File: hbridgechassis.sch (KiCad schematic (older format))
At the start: 8 parts, among them J1 Conn_01x02_Female, J2 Conn_01x02_Female, J3 Conn_01x02_Female, J4 Conn_01x07_Female, J5 Conn_01x02_Female, J6 Conn_01x02_Female, U1 L293DD

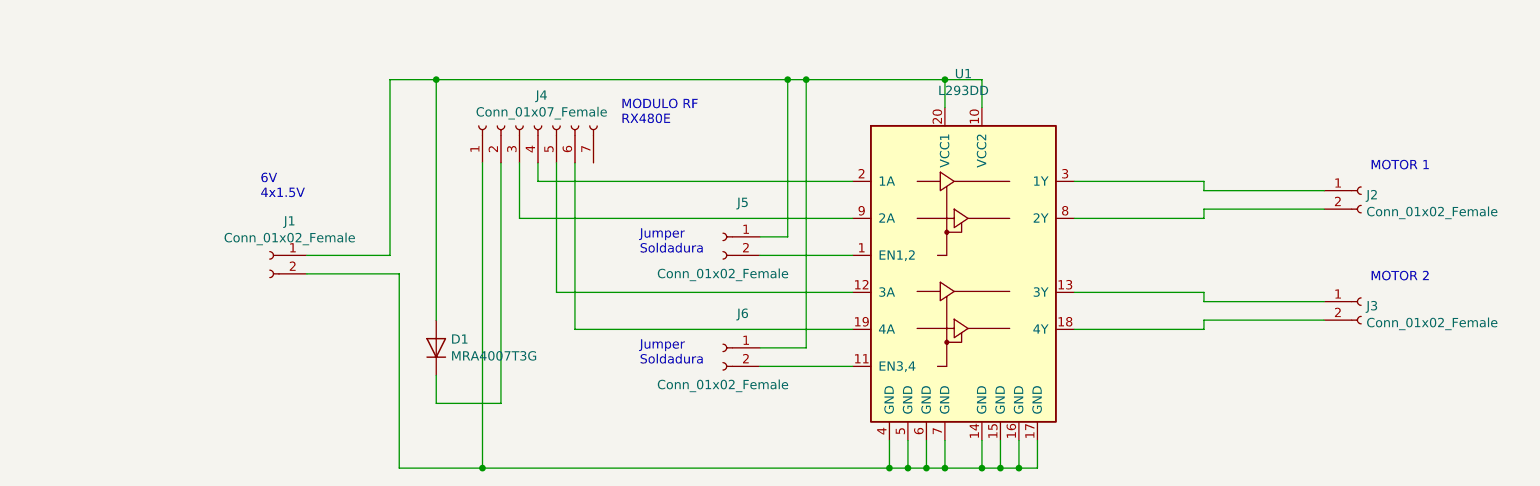
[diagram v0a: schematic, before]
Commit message: agregado regulador 78l05 y condensadores
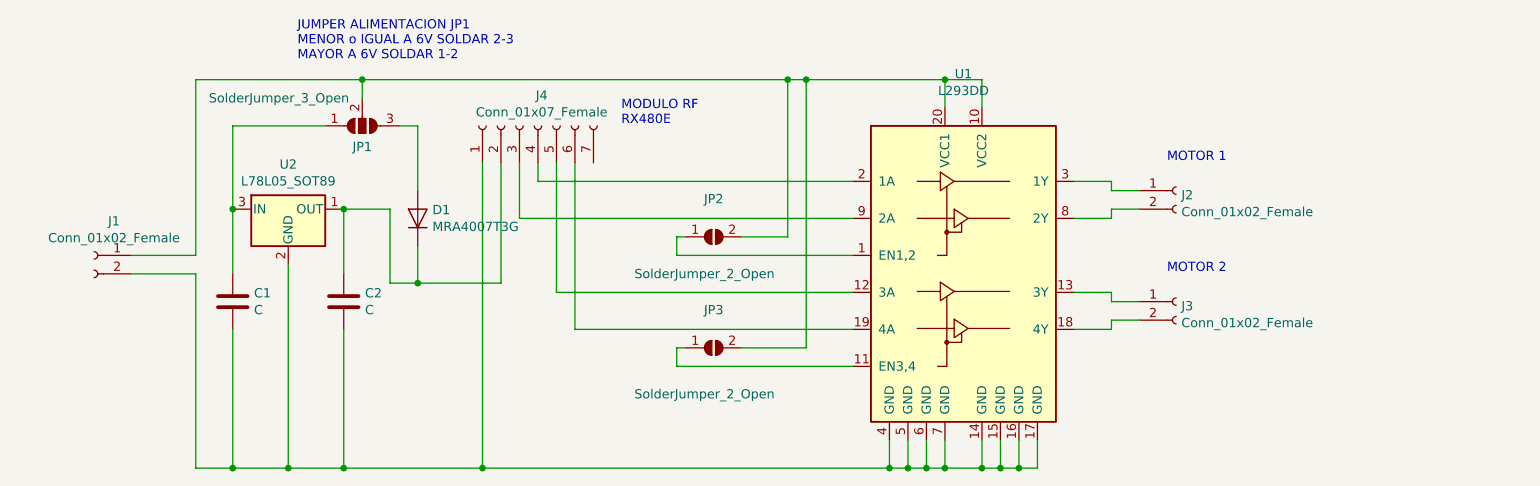
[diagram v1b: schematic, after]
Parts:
- removed J5, J6: Conn_01x02_Female, Jumper:SolderJumper-2_P1.3mm_Open_RoundedPad1.0x1.5mm, symbol Connector:Conn_01x02_Female
- added C1, C2: C, Capacitor_SMD:C_0805_2012Metric, symbol Device:C
- added JP1: SolderJumper_3_Open, Jumper:SolderJumper-3_P1.3mm_Open_RoundedPad1.0x1.5mm_NumberLabels, symbol Jumper:SolderJumper_3_Open
- added JP2, JP3: SolderJumper_2_Open, Jumper:SolderJumper-2_P1.3mm_Open_RoundedPad1.0x1.5mm, symbol Jumper:SolderJumper_2_Open
- added U2: L78L05_SOT89, Package_TO_SOT_SMD:SOT-89-3, symbol Regulator_Linear:L78L05_SOT89
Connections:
- net at U1.1 (EN1,2): now also JP2.1 (A)
- net at J1.1 (Pin_1), U1.10 (VCC2), U1.20 (VCC1): now also JP1.2 (C), JP2.2 (B), JP3.2 (B); no longer D1.2 (A)
- net at U1.11 (EN3,4): now also JP3.1 (A)
- net at J1.2 (Pin_2), J4.1 (Pin_1), U1.14 (GND)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: now also C1.2, C2.2, U2.2 (GND)
- net at D1.1 (K), J4.2 (Pin_2): now also C2.1, U2.1 (OUT)
- new net: C1.1, JP1.1 (A), U2.3 (IN)
- new net: D1.2 (A), JP1.3 (B)
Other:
- note added: "JUMPER ALIMENTACION JP1\nMENOR o IGUAL A 6V SOLDAR 2-3\nMAYOR A 6V SOLDAR 1-2"
- note removed: "6V \n4x1.5V"
- note removed: "Jumper\nSoldadura"
- moved on the sheet: D1, J1, J2, J3
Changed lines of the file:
@@
 L Connector:Conn_01x02_Female J1
 U 1 1 6009FC05
-P 1700 3500
-F 0 "J1" H 1592 3685 50  0000 C CNN
-F 1 "Conn_01x02_Female" H 1592 3594 50  0000 C CNN
-F 2 "TerminalBlock_4Ucon:TerminalBlock_4Ucon_1x02_P3.50mm_Horizontal" H 1700 3500 50  0001 C CNN
-F 3 "~" H 1700 3500 50  0001 C CNN
-	1    1700 3500
+P 750 3500
+F 0 "J1" H 642 3685 50  0000 C CNN
+F 1 "Conn_01x02_Female" H 642 3594 50  0000 C CNN
+F 2 "TerminalBlock_4Ucon:TerminalBlock_4Ucon_1x02_P3.50mm_Horizontal" H 750 3500 50  0001 C CNN
+F 3 "~" H 750 3500 50  0001 C CNN
+	1    750  3500
 	-1   0    0    -1
 $EndComp
@@
 L Connector:Conn_01x02_Female J2
 U 1 1 600A0524
-P 7600 3150
-F 0 "J2" H 7628 3126 50  0000 L CNN
-F 1 "Conn_01x02_Female" H 7628 3035 50  0000 L CNN
-F 2 "TerminalBlock_4Ucon:TerminalBlock_4Ucon_1x02_P3.50mm_Horizontal" H 7600 3150 50  0001 C CNN
-F 3 "~" H 7600 3150 50  0001 C CNN
-	1    7600 3150
+P 6600 3150
+F 0 "J2" H 6628 3126 50  0000 L CNN
+F 1 "Conn_01x02_Female" H 6628 3035 50  0000 L CNN
+F 2 "TerminalBlock_4Ucon:TerminalBlock_4Ucon_1x02_P3.50mm_Horizontal" H 6600 3150 50  0001 C CNN
+F 3 "~" H 6600 3150 50  0001 C CNN
+	1    6600 3150
 	1    0    0    -1
 $EndComp
@@
 L Connector:Conn_01x02_Female J3
 U 1 1 600A0B1B
-P 7600 3750
-F 0 "J3" H 7628 3726 50  0000 L CNN
-F 1 "Conn_01x02_Female" H 7628 3635 50  0000 L CNN
-F 2 "TerminalBlock_4Ucon:TerminalBlock_4Ucon_1x02_P3.50mm_Horizontal" H 7600 3750 50  0001 C CNN
-F 3 "~" H 7600 3750 50  0001 C CNN
-	1    7600 3750
-	1    0    0    -1
-$EndComp
-Wire Wire Line
-	1900 3600 2400 3600
-Wire Wire Line
-	2400 3600 2400 4650
-Wire Wire Line
-	2400 4650 2850 4650
+P 6600 3750
+F 0 "J3" H 6628 3726 50  0000 L CNN
+F 1 "Conn_01x02_Female" H 6628 3635 50  0000 L CNN
+F 2 "TerminalBlock_4Ucon:TerminalBlock_4Ucon_1x02_P3.50mm_Horizontal" H 6600 3750 50  0001 C CNN
+F 3 "~" H 6600 3750 50  0001 C CNN
+	1    6600 3750
+	1    0    0    -1
+$EndComp
+Wire Wire Line
+	950  3600 1300 3600
+Wire Wire Line
+	1300 3600 1300 4650
 Wire Wire Line
 	5050 4650 5050 4500
@@
 Connection ~ 5750 4650
 Wire Wire Line
-	1900 3500 2350 3500
-Wire Wire Line
-	2350 3500 2350 2550
+	950  3500 1300 3500
+Wire Wire Line
+	1300 3500 1300 2550
 Wire Wire Line
 	5350 2550 5350 2700
@@
 	5550 2550 5350 2550
 Connection ~ 5350 2550
-Wire Wire Line
-	7400 3150 6750 3150
-Wire Wire Line
-	6750 3150 6750 3100
-Wire Wire Line
-	6750 3100 6050 3100
-Wire Wire Line
-	7400 3250 6750 3250
-Wire Wire Line
-	6750 3250 6750 3300
-Wire Wire Line
-	6750 3300 6050 3300
-Wire Wire Line
-	7400 3750 6750 3750
-Wire Wire Line
-	6750 3750 6750 3700
-Wire Wire Line
-	6750 3700 6050 3700
-Wire Wire Line
-	7400 3850 6750 3850
-Wire Wire Line
-	6750 3850 6750 3900
-Wire Wire Line
-	6750 3900 6050 3900
 $Comp
 L Connector:Conn_01x07_Female J4
@@
 	0    -1   -1   0
 $EndComp
-$Comp
-L Connector:Conn_01x02_Female J5
-U 1 1 600C3030
-P 4150 3400
-F 0 "J5" H 4042 3585 50  0000 C CNN
-F 1 "Conn_01x02_Female" H 4150 3200 50  0000 C CNN
-F 2 "Jumper:SolderJumper-2_P1.3mm_Open_RoundedPad1.0x1.5mm" H 4150 3400 50  0001 C CNN
-F 3 "~" H 4150 3400 50  0001 C CNN
-	1    4150 3400
-	-1   0    0    -1
-$EndComp
-$Comp
-L Connector:Conn_01x02_Female J6
-U 1 1 600C3816
-P 4150 4000
-F 0 "J6" H 4042 4185 50  0000 C CNN
-F 1 "Conn_01x02_Female" H 4150 3800 50  0000 C CNN
-F 2 "Jumper:SolderJumper-2_P1.3mm_Open_RoundedPad1.0x1.5mm" H 4150 4000 50  0001 C CNN
-F 3 "~" H 4150 4000 50  0001 C CNN
-	1    4150 4000
-	-1   0    0    -1
-$EndComp
-Wire Wire Line
-	4850 3500 4350 3500
-Wire Wire Line
-	4350 3400 4500 3400
 Wire Wire Line
 	4500 3400 4500 2550
@@
 	4500 2550 4600 2550
 Wire Wire Line
-	4850 4100 4350 4100
-Wire Wire Line
-	4350 4000 4600 4000
-Wire Wire Line
 	4600 4000 4600 2550
 Connection ~ 4600 2550
@@
 Wire Wire Line
 	3350 3900 3350 3000
-Wire Wire Line
-	2600 4300 2950 4300
-Wire Wire Line
-	2950 4300 2950 3000
 $Comp
 L Diode:MRA4007T3G D1
 U 1 1 60113E51
-P 2600 4000
-F 0 "D1" V 2646 3921 50  0000 R CNN
-F 1 "MRA4007T3G" V 2555 3921 50  0000 R CNN
-F 2 "Diode_SMD:D_SMA" H 2600 3825 50  0001 C CNN
-F 3 "http://www.onsemi.com/pub_link/Collateral/MRA4003T3-D.PDF" H 2600 4000 50  0001 C CNN
-	1    2600 4000
+P 2500 3300
+F 0 "D1" V 2546 3221 50  0000 R CNN
+F 1 "MRA4007T3G" V 2455 3221 50  0000 R CNN
+F 2 "Diode_SMD:D_SMA" H 2500 3125 50  0001 C CNN
+F 3 "http://www.onsemi.com/pub_link/Collateral/MRA4003T3-D.PDF" H 2500 3300 50  0001 C CNN
+	1    2500 3300
 	0    -1   -1   0
 $EndComp
-Wire Wire Line
-	2350 2550 2600 2550
-Wire Wire Line
-	2600 4150 2600 4300
-Wire Wire Line
-	2600 3850 2600 2550
-Connection ~ 2600 2550
-Wire Wire Line
-	2600 2550 4500 2550
-Text Notes 1650 3200 0    50   ~ 0
-6V \n4x1.5V
 Text Notes 3600 2800 0    50   ~ 0
 MODULO RF\nRX480E
-Text Notes 7650 3050 0    50   ~ 0
+Text Notes 6550 3000 0    50   ~ 0
 MOTOR 1
-Text Notes 7650 3650 0    50   ~ 0
+Text Notes 6550 3600 0    50   ~ 0
 MOTOR 2
-Text Notes 3700 3500 0    50   ~ 0
-Jumper\nSoldadura
-Text Notes 3700 4100 0    50   ~ 0
-Jumper\nSoldadura
+$Comp
+L Regulator_Linear:L78L05_SOT89 U2
+U 1 1 600E16D8
+P 1800 3250
+F 0 "U2" H 1800 3492 50  0000 C CNN
+F 1 "L78L05_SOT89" H 1800 3401 50  0000 C CNN
+F 2 "Package_TO_SOT_SMD:SOT-89-3" H 1800 3450 50  0001 C CIN
+F 3 "http://www.st.com/content/ccc/resource/technical/document/datasheet/15/55/e5/aa/23/5b/43/fd/CD00000446.pdf/files/CD00000446.pdf/jcr:content/translations/en.CD00000446.pdf" H 1800 3200 50  0001 C CNN
+	1    1800 3250
+	1    0    0    -1
+$EndComp
+Wire Wire Line
+	1300 4650 1500 4650
+$Comp
+L Device:C C1
+U 1 1 60125B26
+P 1500 3750
+F 0 "C1" H 1615 3796 50  0000 L CNN
+F 1 "C" H 1615 3705 50  0000 L CNN
+F 2 "Capacitor_SMD:C_0805_2012Metric" H 1538 3600 50  0001 C CNN
+F 3 "~" H 1500 3750 50  0001 C CNN
+	1    1500 3750
+	1    0    0    -1
+$EndComp
+$Comp
+L Device:C C2
+U 1 1 601276C7
+P 2100 3750
+F 0 "C2" H 2215 3796 50  0000 L CNN
+F 1 "C" H 2215 3705 50  0000 L CNN
+F 2 "Capacitor_SMD:C_0805_2012Metric" H 2138 3600 50  0001 C CNN
+F 3 "~" H 2100 3750 50  0001 C CNN
+	1    2100 3750
+	1    0    0    -1
+$EndComp
+Wire Wire Line
+	1800 3550 1800 4650
+Connection ~ 1800 4650
+Wire Wire Line
+	1800 4650 2100 4650
+Wire Wire Line
+	1500 3900 1500 4650
+Connection ~ 1500 4650
+Wire Wire Line
+	1500 4650 1800 4650
+Wire Wire Line
+	2100 3900 2100 4650
+Connection ~ 2100 4650
+Wire Wire Line
+	2100 4650 2850 4650
+Wire Wire Line
+	1500 3600 1500 3250
+Wire Wire Line
+	2100 3600 2100 3250
+$Comp
+L Jumper:SolderJumper_3_Open JP1
+U 1 1 6014A9C6
+P 2200 2800
+F 0 "JP1" H 2200 2913 50  0000 C CNN
+F 1 "SolderJumper_3_Open" H 1750 2650 50  0000 C CNN
+F 2 "Jumper:SolderJumper-3_P1.3mm_Open_RoundedPad1.0x1.5mm_NumberLabels" H 2200 2800 50  0001 C CNN
+F 3 "~" H 2200 2800 50  0001 C CNN
+	1    2200 2800
+	1    0    0    1
+$EndComp
+Wire Wire Line
+	1300 2550 2200 2550
+Wire Wire Line
+	2200 2650 2200 2550
+Connection ~ 2200 2550
+Wire Wire Line
+	2200 2550 4500 2550
+Wire Wire Line
+	2000 2800 1500 2800
+Wire Wire Line
+	1500 2800 1500 3250
+Connection ~ 1500 3250
+Wire Wire Line
+	2350 3650 2500 3650
+Wire Wire Line
+	2950 3000 2950 3650
+Wire Wire Line
+	2500 3650 2500 3450
+Connection ~ 2500 3650
+Wire Wire Line
+	2500 3650 2950 3650
+Wire Wire Line
+	2400 2800 2500 2800
+Wire Wire Line
+	2500 2800 2500 3150
+Wire Wire Line
+	2100 3250 2350 3250
+Wire Wire Line
+	2350 3250 2350 3650
+Connection ~ 2100 3250
+Wire Wire Line
+	6400 3150 6250 3150
+Wire Wire Line
+	6250 3150 6250 3100
+Wire Wire Line
+	6250 3100 6050 3100
+Wire Wire Line
+	6400 3250 6250 3250
+Wire Wire Line
+	6250 3250 6250 3300
+Wire Wire Line
+	6250 3300 6050 3300
+Wire Wire Line
+	6400 3750 6250 3750
+Wire Wire Line
+	6250 3750 6250 3700
+Wire Wire Line
+	6250 3700 6050 3700
+Wire Wire Line
+	6400 3850 6250 3850
+Wire Wire Line
+	6250 3850 6250 3900
+Wire Wire Line
+	6250 3900 6050 3900
+$Comp
+L Jumper:SolderJumper_2_Open JP2
+U 1 1 601CC15D
+P 4100 3400
+F 0 "JP2" H 4100 3605 50  0000 C CNN
+F 1 "SolderJumper_2_Open" H 4050 3200 50  0000 C CNN
+F 2 "Jumper:SolderJumper-2_P1.3mm_Open_RoundedPad1.0x1.5mm" H 4100 3400 50  0001 C CNN
+F 3 "~" H 4100 3400 50  0001 C CNN
+	1    4100 3400
+	1    0    0    -1
+$EndComp
+$Comp
+L Jumper:SolderJumper_2_Open JP3
+U 1 1 601CCD9F
+P 4100 4000
+F 0 "JP3" H 4100 4205 50  0000 C CNN
+F 1 "SolderJumper_2_Open" H 4050 3750 50  0000 C CNN
+F 2 "Jumper:SolderJumper-2_P1.3mm_Open_RoundedPad1.0x1.5mm" H 4100 4000 50  0001 C CNN
+F 3 "~" H 4100 4000 50  0001 C CNN
+	1    4100 4000
+	1    0    0    -1
+$EndComp
+Wire Wire Line
+	4250 3400 4500 3400
+Wire Wire Line
+	3950 3400 3900 3400
+Wire Wire Line
+	3900 3400 3900 3500
+Wire Wire Line
+	3900 3500 4850 3500
+Wire Wire Line
+	4250 4000 4600 4000
+Wire Wire Line
+	3950 4000 3900 4000
+Wire Wire Line
+	3900 4000 3900 4100
+Wire Wire Line
+	3900 4100 4850 4100
+Text Notes 1850 2450 0    50   ~ 0
+JUMPER ALIMENTACION JP1\nMENOR o IGUAL A 6V SOLDAR 2-3\nMAYOR A 6V SOLDAR 1-2
 $EndSCHEMATC

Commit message: enrutado preliminar de pistas y archivos de fabricacion
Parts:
- C1: value C -> 0.33uF
- C2: value C -> 0.1uF
- J1, J2, J3: value Conn_01x02_Female -> 3.5 mm screw terminal
- J4: value Conn_01x07_Female -> 2.54 mm 01x07 Female socket
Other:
- note added: "MOTOR A"
- note added: "MOTOR B"
- note removed: "MOTOR 1"
- note removed: "MOTOR 2"
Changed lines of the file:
@@
 P 750 3500
 F 0 "J1" H 642 3685 50  0000 C CNN
-F 1 "Conn_01x02_Female" H 642 3594 50  0000 C CNN
+F 1 "3.5 mm screw terminal" H 642 3594 50  0000 C CNN
 F 2 "TerminalBlock_4Ucon:TerminalBlock_4Ucon_1x02_P3.50mm_Horizontal" H 750 3500 50  0001 C CNN
 F 3 "~" H 750 3500 50  0001 C CNN
@@
 P 6600 3150
 F 0 "J2" H 6628 3126 50  0000 L CNN
-F 1 "Conn_01x02_Female" H 6628 3035 50  0000 L CNN
+F 1 "3.5 mm screw terminal" H 6628 3035 50  0000 L CNN
 F 2 "TerminalBlock_4Ucon:TerminalBlock_4Ucon_1x02_P3.50mm_Horizontal" H 6600 3150 50  0001 C CNN
 F 3 "~" H 6600 3150 50  0001 C CNN
@@
 P 6600 3750
 F 0 "J3" H 6628 3726 50  0000 L CNN
-F 1 "Conn_01x02_Female" H 6628 3635 50  0000 L CNN
+F 1 "3.5 mm screw terminal" H 6628 3635 50  0000 L CNN
 F 2 "TerminalBlock_4Ucon:TerminalBlock_4Ucon_1x02_P3.50mm_Horizontal" H 6600 3750 50  0001 C CNN
 F 3 "~" H 6600 3750 50  0001 C CNN
@@
 P 3150 2800
 F 0 "J4" V 3315 2780 50  0000 C CNN
-F 1 "Conn_01x07_Female" V 3224 2780 50  0000 C CNN
+F 1 "2.54 mm 01x07 Female socket" V 3224 2780 50  0000 C CNN
 F 2 "Connector_PinSocket_2.54mm:PinSocket_1x07_P2.54mm_Vertical" H 3150 2800 50  0001 C CNN
 F 3 "~" H 3150 2800 50  0001 C CNN
@@
 MODULO RF\nRX480E
 Text Notes 6550 3000 0    50   ~ 0
-MOTOR 1
+MOTOR A
 Text Notes 6550 3600 0    50   ~ 0
-MOTOR 2
+MOTOR B
 $Comp
 L Regulator_Linear:L78L05_SOT89 U2
@@
 P 1500 3750
 F 0 "C1" H 1615 3796 50  0000 L CNN
-F 1 "C" H 1615 3705 50  0000 L CNN
+F 1 "0.33uF" H 1615 3705 50  0000 L CNN
 F 2 "Capacitor_SMD:C_0805_2012Metric" H 1538 3600 50  0001 C CNN
 F 3 "~" H 1500 3750 50  0001 C CNN
@@
 P 2100 3750
 F 0 "C2" H 2215 3796 50  0000 L CNN
-F 1 "C" H 2215 3705 50  0000 L CNN
+F 1 "0.1uF" H 2215 3705 50  0000 L CNN
 F 2 "Capacitor_SMD:C_0805_2012Metric" H 2138 3600 50  0001 C CNN
 F 3 "~" H 2100 3750 50  0001 C CNN

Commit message: Logo, areas de cobre y mejoras en serigrafia
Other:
- note added: "JUMPER ALIMENTACION JP1\nMENOR o IGUAL A 6V SOLDAR 3-2\nMAYOR A 6V SOLDAR 2-1"
- note removed: "JUMPER ALIMENTACION JP1\nMENOR o IGUAL A 6V SOLDAR 2-3\nMAYOR A 6V SOLDAR 1-2"
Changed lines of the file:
@@
 	3900 4100 4850 4100
 Text Notes 1850 2450 0    50   ~ 0
-JUMPER ALIMENTACION JP1\nMENOR o IGUAL A 6V SOLDAR 2-3\nMAYOR A 6V SOLDAR 1-2
+JUMPER ALIMENTACION JP1\nMENOR o IGUAL A 6V SOLDAR 3-2\nMAYOR A 6V SOLDAR 2-1
 $EndSCHEMATC
